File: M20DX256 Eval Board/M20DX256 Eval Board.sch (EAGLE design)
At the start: 24 parts, among them J1 M52-040000S0545, J2 20_PIN, J3 20_PIN, SW1 KMR211G, U1 MK20DX256VLH7, Y1 8MHz, Y2 32.768kHz, 12.5pF

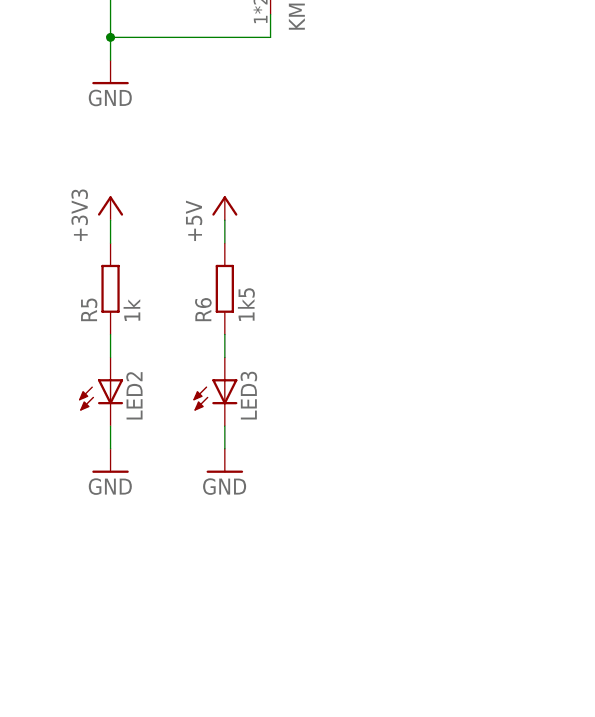
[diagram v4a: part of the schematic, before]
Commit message: Add test pad and curve the corner of the board
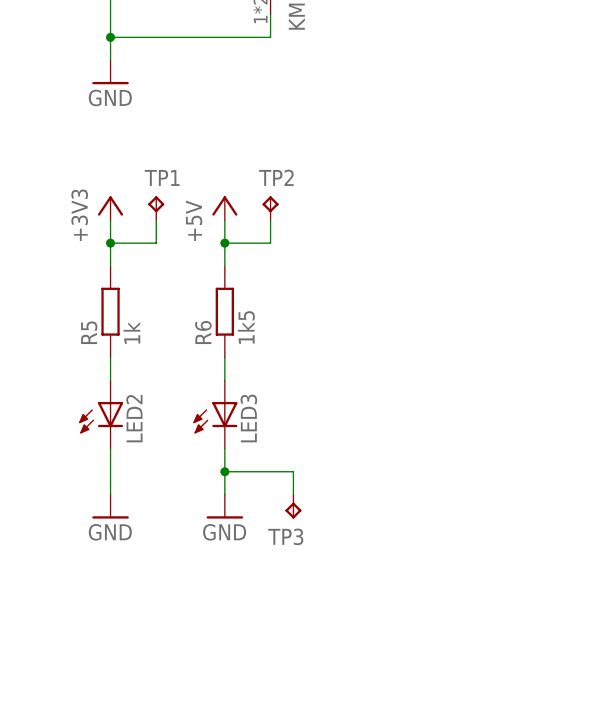
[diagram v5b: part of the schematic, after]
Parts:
- added TP1, TP2, TP3: TPB1,27, testpad:TPB1,27
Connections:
- net +3V3: now also TP1.TP
- net +5V: now also TP2.TP
- net GND: now also TP3.TP
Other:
- moved on the sheet: LED2, LED3, R5, R6
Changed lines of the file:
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@@
 <part name="LED2" library="led" deviceset="LED" device="CHIP-LED0603"/>
 <part name="LED3" library="led" deviceset="LED" device="CHIP-LED0603"/>
+<part name="TP1" library="testpad" deviceset="TP" device="B1,27"/>
+<part name="TP2" library="testpad" deviceset="TP" device="B1,27"/>
+<part name="TP3" library="testpad" deviceset="TP" device="B1,27"/>
 </parts>
 <sheets>
@@
 <instance part="P+4" gate="1" x="337.82" y="195.58"/>
 <instance part="+3V11" gate="G$1" x="15.24" y="124.46"/>
-<instance part="R5" gate="G$1" x="15.24" y="114.3" rot="R90"/>
-<instance part="GND8" gate="1" x="15.24" y="93.98"/>
-<instance part="GND12" gate="1" x="27.94" y="93.98"/>
-<instance part="R6" gate="G$1" x="27.94" y="114.3" rot="R90"/>
+<instance part="R5" gate="G$1" x="15.24" y="111.76" rot="R90"/>
+<instance part="GND8" gate="1" x="15.24" y="88.9"/>
+<instance part="GND12" gate="1" x="27.94" y="88.9"/>
+<instance part="R6" gate="G$1" x="27.94" y="111.76" rot="R90"/>
 <instance part="P+3" gate="1" x="27.94" y="124.46"/>
-<instance part="LED2" gate="G$1" x="15.24" y="104.14"/>
-<instance part="LED3" gate="G$1" x="27.94" y="104.14"/>
+<instance part="LED2" gate="G$1" x="15.24" y="101.6"/>
+<instance part="LED3" gate="G$1" x="27.94" y="101.6"/>
+<instance part="TP1" gate="G$1" x="20.32" y="124.46"/>
+<instance part="TP2" gate="G$1" x="33.02" y="124.46"/>
+<instance part="TP3" gate="G$1" x="35.56" y="88.9" rot="R180"/>
 </instances>
 <busses>
@@
 <pinref part="R5" gate="G$1" pin="2"/>
 <pinref part="+3V11" gate="G$1" pin="+3V3"/>
+<wire x1="15.24" y1="116.84" x2="15.24" y2="119.38" width="0.1524" layer="91"/>
+<pinref part="TP1" gate="G$1" pin="TP"/>
 <wire x1="15.24" y1="119.38" x2="15.24" y2="121.92" width="0.1524" layer="91"/>
+<wire x1="15.24" y1="119.38" x2="20.32" y2="119.38" width="0.1524" layer="91"/>
+<wire x1="20.32" y1="119.38" x2="20.32" y2="121.92" width="0.1524" layer="91"/>
+<junction x="15.24" y="119.38"/>
 </segment>
 </net>
@@
 <pinref part="GND8" gate="1" pin="GND"/>
 <pinref part="LED2" gate="G$1" pin="C"/>
-<wire x1="15.24" y1="96.52" x2="15.24" y2="99.06" width="0.1524" layer="91"/>
+<wire x1="15.24" y1="91.44" x2="15.24" y2="96.52" width="0.1524" layer="91"/>
 </segment>
 <segment>
 <pinref part="GND12" gate="1" pin="GND"/>
 <pinref part="LED3" gate="G$1" pin="C"/>
-<wire x1="27.94" y1="96.52" x2="27.94" y2="99.06" width="0.1524" layer="91"/>
+<wire x1="27.94" y1="91.44" x2="27.94" y2="93.98" width="0.1524" layer="91"/>
+<pinref part="TP3" gate="G$1" pin="TP"/>
+<wire x1="27.94" y1="93.98" x2="27.94" y2="96.52" width="0.1524" layer="91"/>
+<wire x1="27.94" y1="93.98" x2="35.56" y2="93.98" width="0.1524" layer="91"/>
+<wire x1="35.56" y1="93.98" x2="35.56" y2="91.44" width="0.1524" layer="91"/>
+<junction x="27.94" y="93.98"/>
 </segment>
 </net>
@@
 <pinref part="R6" gate="G$1" pin="2"/>
 <pinref part="P+3" gate="1" pin="+5V"/>
+<wire x1="27.94" y1="116.84" x2="27.94" y2="119.38" width="0.1524" layer="91"/>
+<pinref part="TP2" gate="G$1" pin="TP"/>
 <wire x1="27.94" y1="119.38" x2="27.94" y2="121.92" width="0.1524" layer="91"/>
+<wire x1="27.94" y1="119.38" x2="33.02" y2="119.38" width="0.1524" layer="91"/>
+<wire x1="33.02" y1="119.38" x2="33.02" y2="121.92" width="0.1524" layer="91"/>
+<junction x="27.94" y="119.38"/>
 </segment>
 </net>
@@
 <pinref part="LED3" gate="G$1" pin="A"/>
 <pinref part="R6" gate="G$1" pin="1"/>
-<wire x1="27.94" y1="106.68" x2="27.94" y2="109.22" width="0.1524" layer="91"/>
+<wire x1="27.94" y1="104.14" x2="27.94" y2="106.68" width="0.1524" layer="91"/>
 </segment>
 </net>
@@
 <pinref part="LED2" gate="G$1" pin="A"/>
 <pinref part="R5" gate="G$1" pin="1"/>
-<wire x1="15.24" y1="106.68" x2="15.24" y2="109.22" width="0.1524" layer="91"/>
-</segment>
-</net>
+<wire x1="15.24" y1="104.14" x2="15.24" y2="106.68" width="0.1524" layer="91"/>
+</segment>
+</net>

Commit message: Add fiducial
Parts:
- added JP1, JP2, JP3, JP4: FIDUCIAL1X2, SparkFun:FIDUCIAL1X2
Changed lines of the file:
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@@
 <part name="TP2" library="testpad" deviceset="TP" device="B1,27"/>
 <part name="TP3" library="testpad" deviceset="TP" device="B1,27"/>
+<part name="JP1" library="SparkFun" deviceset="FIDUCIAL" device="1X2"/>
+<part name="JP2" library="SparkFun" deviceset="FIDUCIAL" device="1X2"/>
+<part name="JP3" library="SparkFun" deviceset="FIDUCIAL" device="1X2"/>
+<part name="JP4" library="SparkFun" deviceset="FIDUCIAL" device="1X2"/>
 </parts>
 <sheets>
@@
 <instance part="TP2" gate="G$1" x="33.02" y="124.46"/>
 <instance part="TP3" gate="G$1" x="35.56" y="88.9" rot="R180"/>
+<instance part="JP1" gate="G$1" x="378.46" y="27.94"/>
+<instance part="JP2" gate="G$1" x="373.38" y="27.94"/>
+<instance part="JP3" gate="G$1" x="368.3" y="27.94"/>
+<instance part="JP4" gate="G$1" x="363.22" y="27.94"/>
 </instances>
 <busses>

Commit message: Add name of the board, CC, and logo of exmachina
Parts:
- added U$2: CC-BY-SA, cc-by-sa:CC-BY-SA
- added U$3: EXMACHINA-LOGO-NAME, exmachina:EXMACHINA-LOGO-NAME
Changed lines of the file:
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@@
 <part name="JP3" library="SparkFun" deviceset="FIDUCIAL" device="1X2"/>
 <part name="JP4" library="SparkFun" deviceset="FIDUCIAL" device="1X2"/>
+<part name="U$2" library="cc-by-sa" deviceset="CC-BY-SA" device=""/>
+<part name="U$3" library="exmachina" deviceset="EXMACHINA-LOGO" device="-NAME"/>
 </parts>
 <sheets>
@@
 <instance part="JP3" gate="G$1" x="368.3" y="27.94"/>
 <instance part="JP4" gate="G$1" x="363.22" y="27.94"/>
+<instance part="U$2" gate="A" x="303.784" y="8.89"/>
+<instance part="U$3" gate="G$1" x="311.404" y="18.796"/>
 </instances>
 <busses>

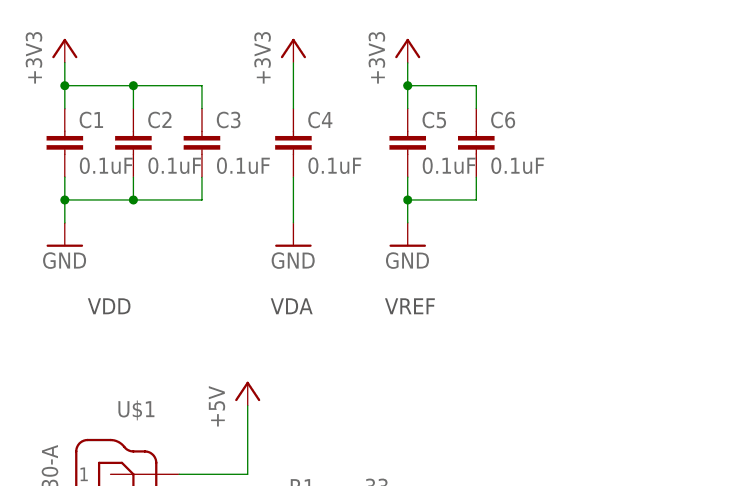
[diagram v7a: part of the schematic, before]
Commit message: Deleted C4 and C5 Renaming C6 to C4
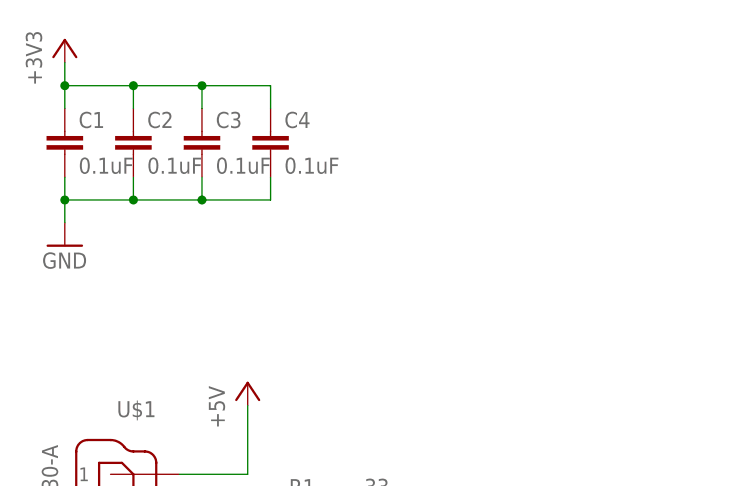
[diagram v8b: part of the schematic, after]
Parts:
- removed C5, C6: 0.1uF, rcl:C-EUC0603
- C1, C2, C3, C4, C7: MPN (none) -> MC0603B104K160CT; OC_NEWARK (none) -> 06R4923
- J1: MPN (none) -> M52-040000S0545; OC_NEWARK (none) -> 97K6309
- J2, J3, JP1, JP2, JP3, JP4, LED1, LED2, LED3, TP1, TP2, TP3, U$2, U$3: OC_NEWARK (none) -> unknown
- R1, R2: MPN (none) -> MCMR06X33R0FTL; OC_NEWARK (none) -> 86T3614
- R3: MPN (none) -> MCMR06X1002FTL; OC_NEWARK (none) -> 86T3506
- R4, R5: MPN (none) -> MCMR06X1001FTL; OC_NEWARK (none) -> 86T3505
- R6: MPN (none) -> MCMR06X1501FTL; OC_NEWARK (none) -> 86T3542
- SW1: MPN (none) -> KMR211G LFS; OC_NEWARK (none) -> 58M7852
- U$1: MPN (none) -> USB3075-30-A; OC_NEWARK (none) -> 58T0863
- Y1: MPN (none) -> CSTCE8M00G55Z-R0; OC_NEWARK (none) -> 80P4001
- Y2: MPN (none) -> ABS07-32.768KHZ-1-T; OC_NEWARK (none) -> 11N6974
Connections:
- net +3V3: no longer C5.1, C6.1
- net GND: no longer C5.2, C6.2
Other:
- note removed: "VDA"
- note removed: "VDD"
- note removed: "VREF"
- moved on the sheet: C4
